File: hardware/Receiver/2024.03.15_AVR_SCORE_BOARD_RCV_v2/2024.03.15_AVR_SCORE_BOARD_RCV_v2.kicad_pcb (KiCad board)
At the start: 2 copper layers, 36 parts, among them J1 ARK_01x03, J3 UART, J4 Conn_01x03, J5 Conn_01x03, J6 Conn_01x03, U1 ATmega328P-PU, U2 AIMTEC_AMSROL-78NZ, U3 NRF24l04, U4 PCF8563T, U5 Kanda_ISP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

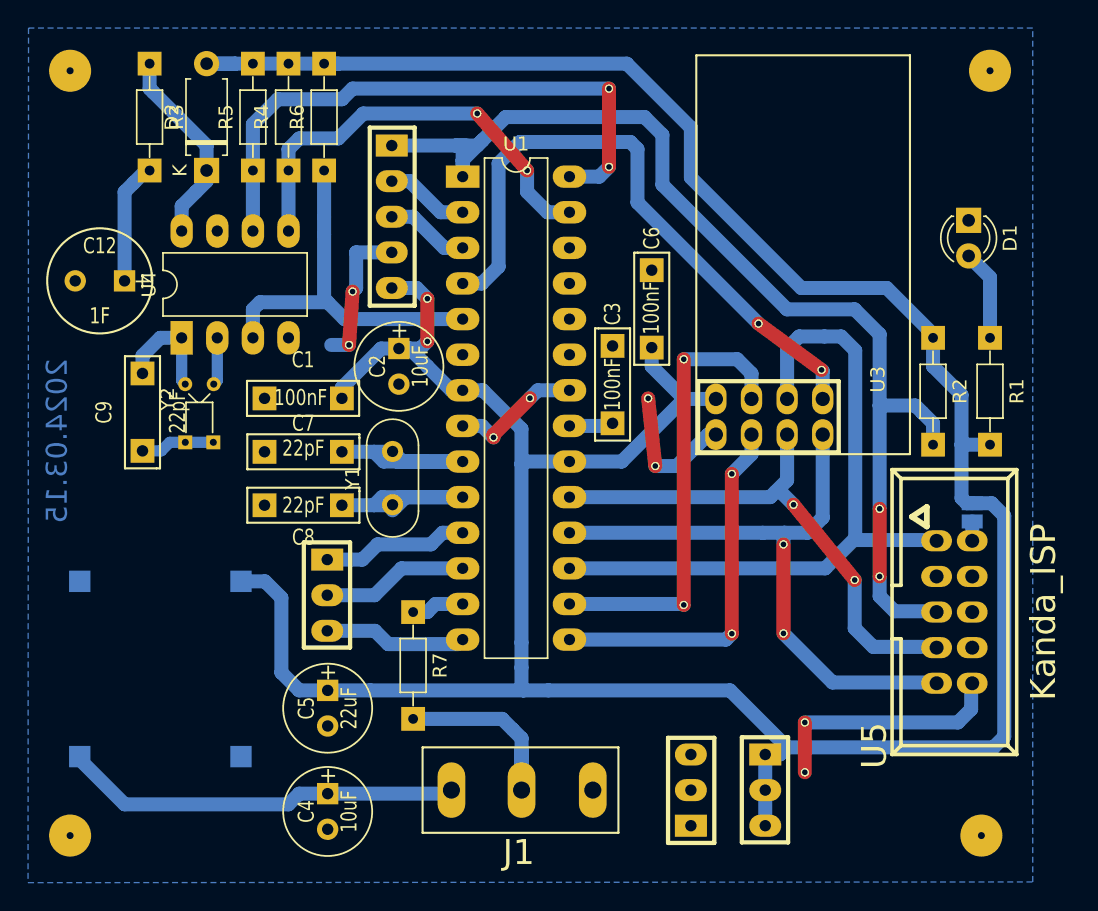
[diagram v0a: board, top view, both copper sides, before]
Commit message: change design to 5v logic level
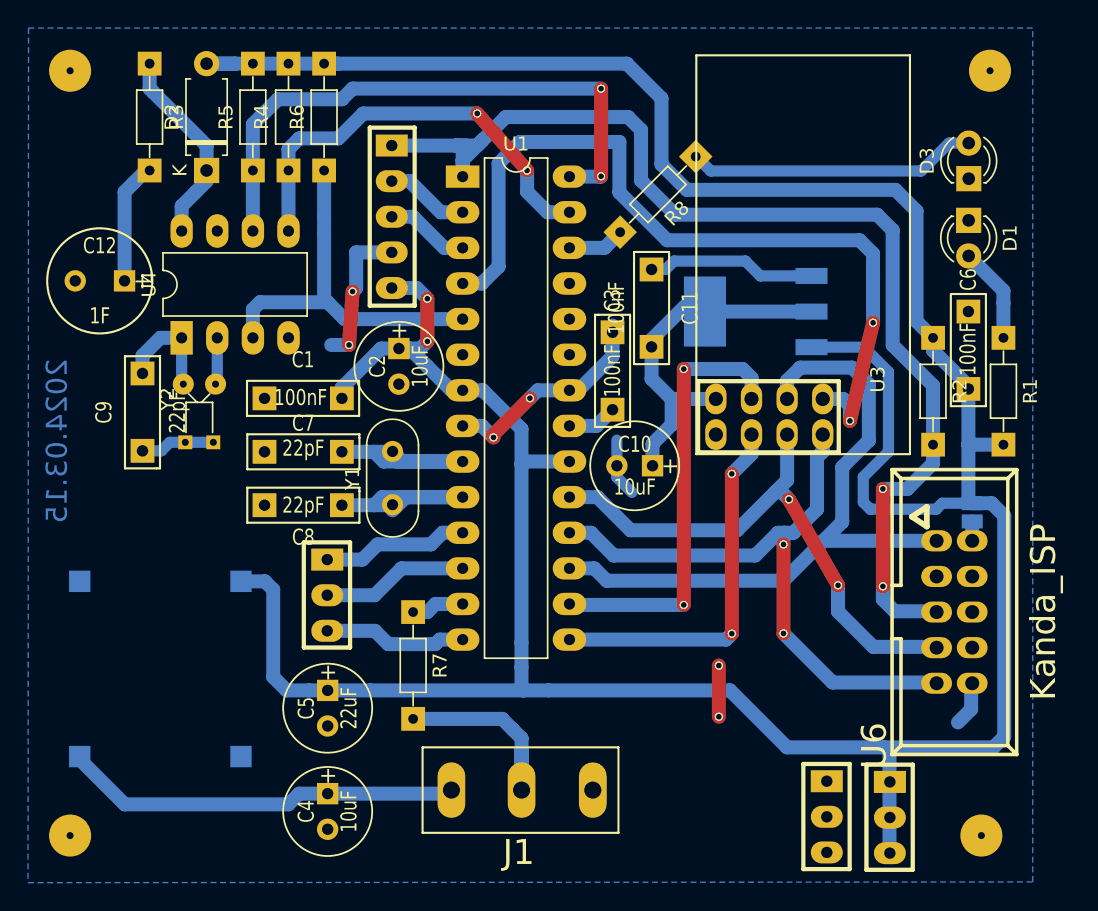
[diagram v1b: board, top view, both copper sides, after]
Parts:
- added C10: 10uF, Moje:C(2,5mm), F.Cu at (69.4, 58.4)
- added C11: 100nF, Moje:C[5,5mm], F.Cu at (70.6, 47.1)
- added D3: LED, LED_THT:LED_D3.0mm, F.Cu at (93.2, 37.9)
- added R8: 1k, Moje:R_MY_DIN0204_L3.6mm_D1.6mm_P7.62mm, F.Cu at (73.8, 36.4)
- added U5: LM1117, Moje:TO263_MY, B.Cu at (78.2, 47.4)
- moved C6 22.8 mm to (93.2, 50.1)
- moved J6 9.91 mm to (83.1, 83.4), turned to 270 degrees
- moved J5 9.10 mm to (87.6, 83.4)
- moved C3 0.97 mm to (67.8, 51.6)
- moved R1 0.96 mm to (95.7, 49.3)
- renumbered U5 to U6
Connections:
- C1 pad 1: +3V3 -> +5V
- C2 pad 1: +3V3 -> +5V
- C5 pad 1: +3V3 -> +5V
- C6 pad 1: +3V3 -> +5V
- D2 pad 2: +3V3 -> +5V
- J3 pad 5: +3V3 -> +5V
- J5 pad 1: +3V3 -> +5V
- J5 pad 2: +3V3 -> +5V
- J5 pad 3: +3V3 -> +5V
- JP1 pad 1: +3V3 -> +5V
- R1 pad 2: +3V3 -> +5V
- R2 pad 1: +3V3 -> +5V
- R4 pad 2: +3V3 -> +5V
- R5 pad 2: +3V3 -> +5V
- R6 pad 2: +3V3 -> +5V
- U1 pad 20: +3V3 -> +5V
- U1 pad 7: +3V3 -> +5V
- U2 pad 3: +3V3 -> +5V
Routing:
- net +5V: track 0.00 -> 248.1 mm, vias 0 -> 2
- net +3V3: track 234.1 -> 25.6 mm, vias 2 -> 0
- net Net-(D3-Pad2): track 0.00 -> 20.7 mm
- net INT0_NRF: track 44.9 -> 58.5 mm
- net Net-(R8-Pad2): track 0.00 -> 4.08 mm
- net RST: track 79.0 -> 82.1 mm
- net SCK: track 37.6 -> 39.4 mm
- net GND: track 53.1 -> 54.7 mm, vias 8 -> 6
- net MOSI: track 49.7 -> 48.2 mm
- net SS: track 32.8 -> 31.6 mm
- net CE: track 26.5 -> 27.4 mm
- net MISO: track 43.9 -> 44.7 mm
- net SCL: track 43.3 -> 42.5 mm
